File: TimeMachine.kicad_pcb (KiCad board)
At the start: 4 copper layers, 107.6 x 59.8 mm, 52 parts, among them J1 AppleIIBus, J2 JTAG, U1 EPM7128SL84, U2 DS1215, U3 74AHCT04, U4 AS6C8008, U5 39F040, Y1 32k768

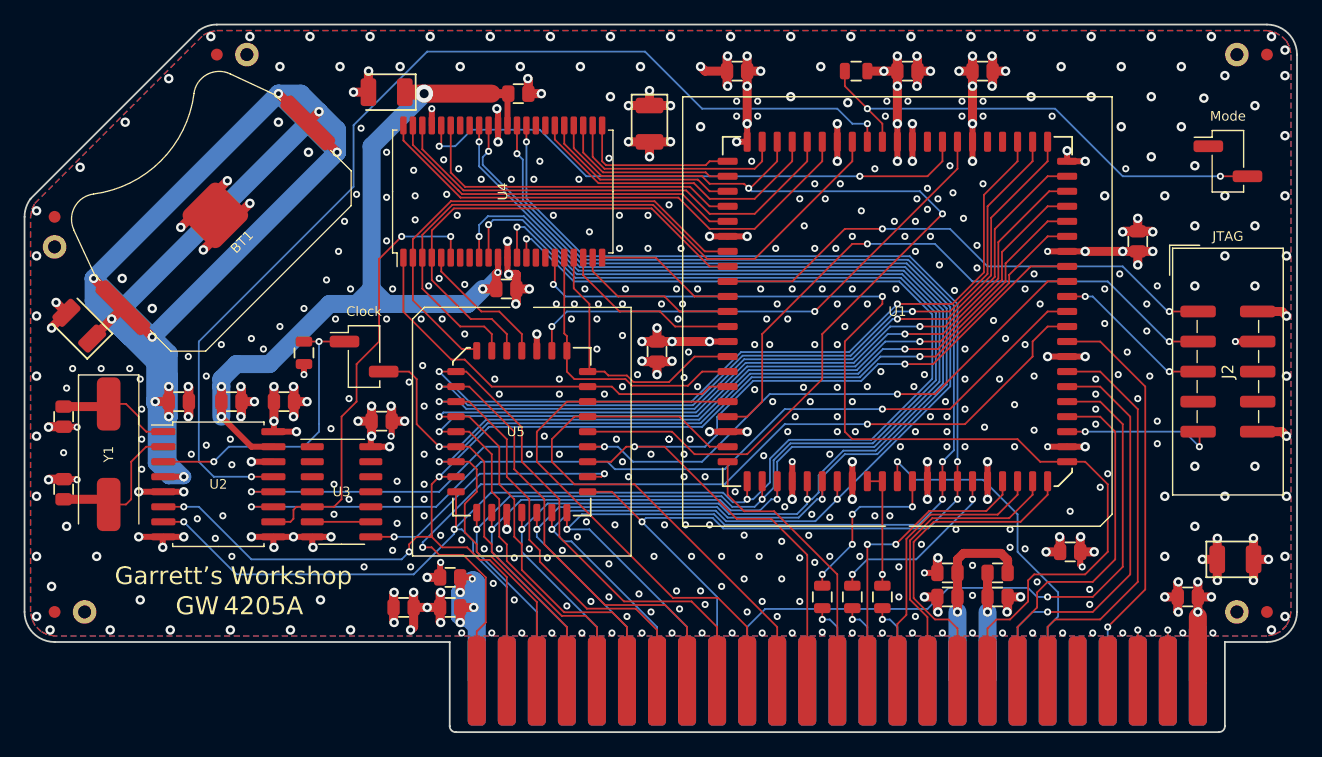
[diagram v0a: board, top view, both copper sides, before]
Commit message: Buffered data bus with CPLD
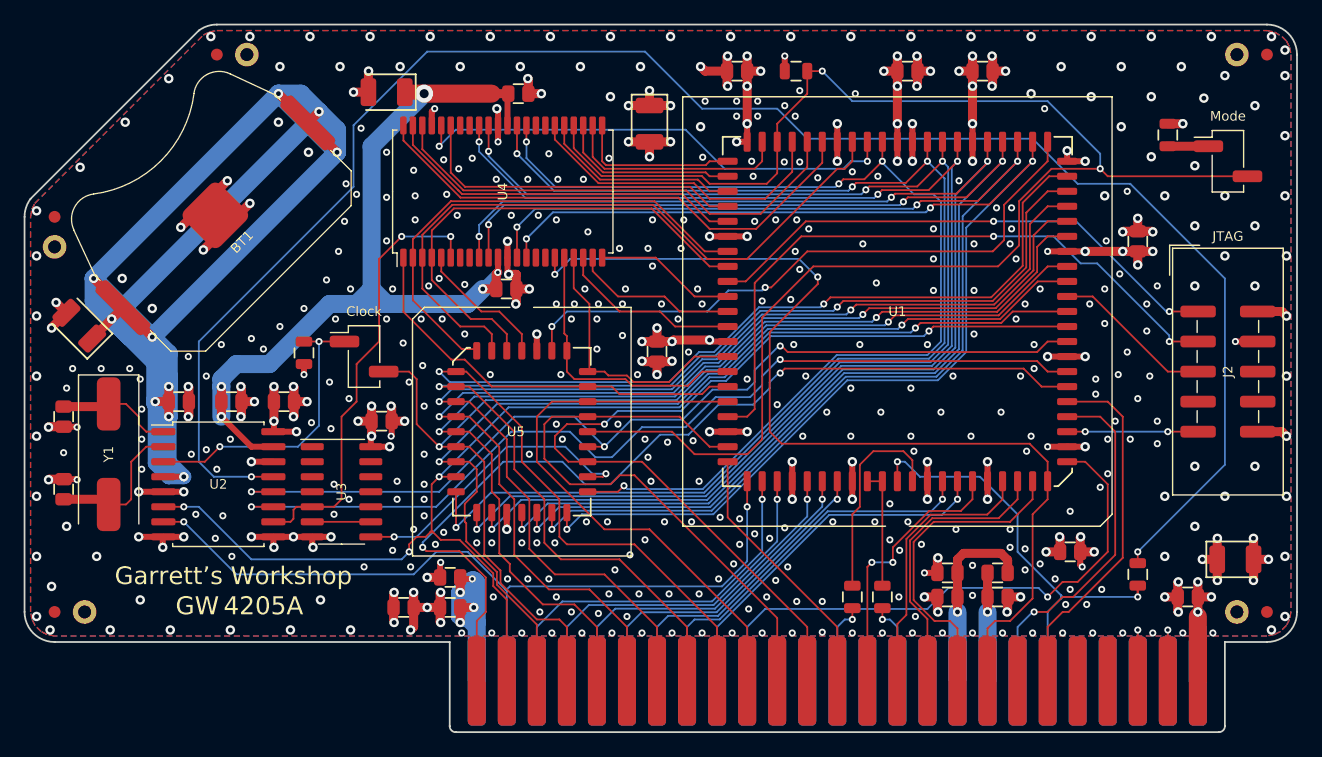
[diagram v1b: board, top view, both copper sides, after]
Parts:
- added R6: 4k7, stdpads:R_0805, F.Cu at (233.7, 126.4)
- R2: value 100 -> 22k
- U3: footprint Package_SO:SOIC-14_3.9x8.7mm_P1.27mm -> stdpads:SOIC-14_3.9mm
- moved R2 44.7 mm to (204.8, 83.8), turned to 0 degrees
- moved R5 26.9 mm to (236.2, 89.2), turned to 90 degrees
- moved R1 2.54 mm to (209.6, 128.3)
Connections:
- net /RAMROMCSgb renamed Net-(U3-Pad6)
- J1 pad 19: /SYNC -> /VIDSYNC
- JP1 pad 1: GND -> Net-(JP1-Pad1)
- JP1 pad 2: /~SMode~ -> /RA11
- R2 pad 1: /Q3r -> GND
- R2 pad 2: /Q3 -> /RA11
- R5 pad 1: /~SMode~ -> Net-(JP1-Pad1)
- U1 pad 10: /A14 -> /A15
- U1 pad 11: /A15 -> /R~W~
- U1 pad 12: /R~W~ -> /~DEVSEL~
- U1 pad 15: /SYNC -> /~INH~
- U1 pad 16: /~DEVSEL~ -> /~IOSTRB~
- U1 pad 17: /~INH~ -> /~IOSEL~
- U1 pad 18: /~IOSTRB~ -> /RAMROM~CS~
- U1 pad 20: /~NMI~ -> /ROM~OE~
- U1 pad 21: /~IOSEL~ -> /A10
- U1 pad 22: /RAMROM~CS~ -> /A0
- U1 pad 24: /ROM~OE~ -> /A1
- U1 pad 25: /A10 -> /A2
- U1 pad 27: /A0 -> /A3
- U1 pad 28: /A1 -> /A4
- U1 pad 29: /A2 -> /A5
- U1 pad 30: /A3 -> /A6
- U1 pad 31: /A4 -> /A7
- U1 pad 33: /A5 -> /ROM~WE~
- U1 pad 34: /A6 -> /RD6
- U1 pad 35: /A7 -> /RD5
- U1 pad 36: Net-(U1-Pad36) -> /RD4
- U1 pad 37: Net-(U1-Pad37) -> /RD3
- U1 pad 39: /ROM~WE~ -> /RD2
- U1 pad 40: /RAMCS -> /RD1
- U1 pad 41: Net-(U1-Pad41) -> /RD0
- U1 pad 44: /~SMode~ -> /RD7
- U1 pad 45: /C~RES~ -> /RAMCS
- U1 pad 6: /Q3r -> /A12
- U1 pad 8: /A12 -> /A13
- U1 pad 9: /A13 -> /A14
- U4 pad 10: /D2 -> /RD4
- U4 pad 13: /D1 -> /RD5
- U4 pad 14: /D0 -> /RD6
- U4 pad 31: /D7 -> /RD7
- U4 pad 32: /D6 -> /RD0
- U4 pad 35: /D5 -> /RD1
- U4 pad 36: /D4 -> /RD2
- U4 pad 9: /D3 -> /RD3
- U5 pad 13: /D0 -> /RD0
- U5 pad 14: /D1 -> /RD1
- U5 pad 15: /D2 -> /RD2
- U5 pad 17: /D3 -> /RD3
- U5 pad 18: /D4 -> /RD4
- U5 pad 19: /D5 -> /RD5
- U5 pad 20: /D6 -> /RD6
- U5 pad 21: /D7 -> /RD7
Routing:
- net /RD4: track 0.00 -> 111.1 mm, vias 0 -> 4
- net /RD3: track 0.00 -> 111.0 mm, vias 0 -> 4
- net /RD2: track 0.00 -> 109.7 mm, vias 0 -> 4
- net /RD5: track 0.00 -> 109.2 mm, vias 0 -> 4
- net /RD6: track 0.00 -> 108.6 mm, vias 0 -> 4
- net /RD1: track 0.00 -> 108.5 mm, vias 0 -> 4
- net /RD0: track 0.00 -> 107.9 mm, vias 0 -> 4
- net /RD7: track 0.00 -> 90.0 mm, vias 0 -> 4
- net /D5: track 114.0 -> 25.8 mm, vias 3 -> 1
- net /D4: track 114.9 -> 27.4 mm, vias 3 -> 1
- net /D6: track 116.6 -> 32.2 mm, vias 4 -> 1
- net /D2: track 114.2 -> 30.4 mm, vias 3 -> 1
- net /D3: track 112.7 -> 29.2 mm, vias 3 -> 1
- net /D7: track 112.8 -> 30.9 mm, vias 4 -> 1
- net /D1: track 110.7 -> 32.2 mm, vias 3 -> 1
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
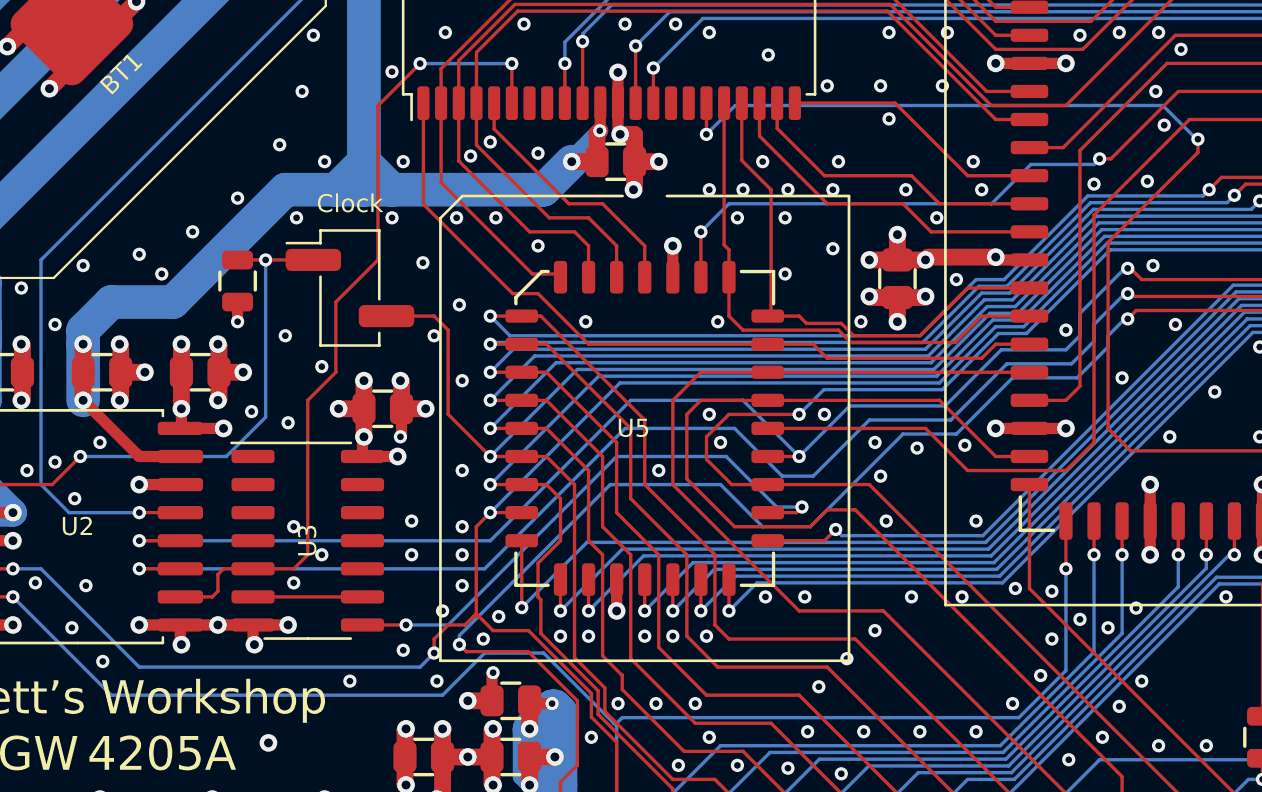
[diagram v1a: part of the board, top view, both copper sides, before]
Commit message: Changed ROM OE strategy
Has gerbers submitted to JLCPCB though
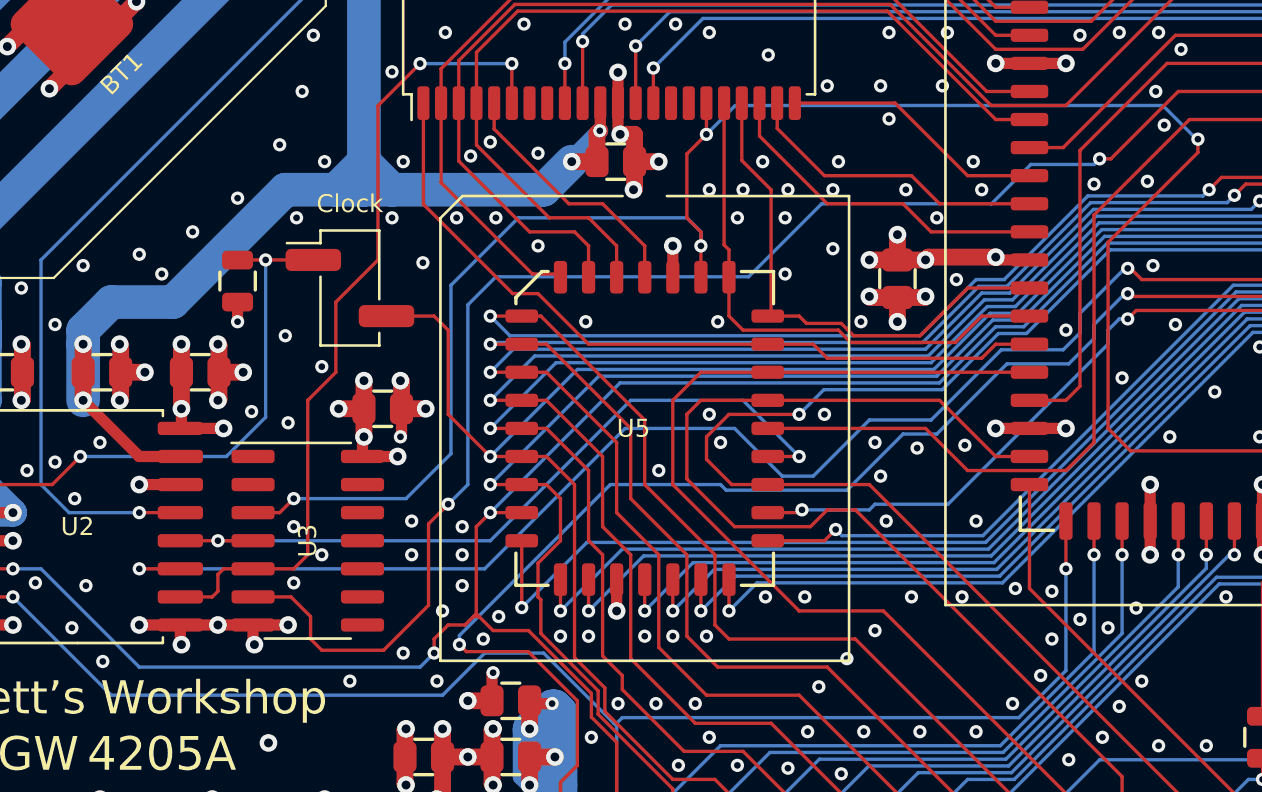
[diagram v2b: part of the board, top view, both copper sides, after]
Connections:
- U1 pad 17: /~IOSEL~ -> /ROM~CS~
- U1 pad 18: /RAMROM~CS~ -> /~IOSEL~
- U1 pad 20: /ROM~OE~ -> /RAMROM~CS~
- U1 pad 33: /ROM~WE~ -> /RAMROMCSgb
- U2 pad 12: /ROM~OE~ -> /~OE~
- U3 pad 3: GND -> /R~W~
- U3 pad 4: Net-(U3-Pad4) -> /~OE~
- U3 pad 6: Net-(U3-Pad6) -> /RAMROMCSgb
- U3 pad 8: /RAMROM~CS~gb -> Net-(U3-Pad8)
- U3 pad 9: Net-(U3-Pad6) -> GND
- U5 pad 22: /RAMROM~CS~gb -> /ROM~CS~
- U5 pad 24: /ROM~OE~ -> /~OE~
- U5 pad 31: /ROM~WE~ -> /R~W~
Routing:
- net /RAMROMCSgb: track 0.00 -> 87.7 mm, vias 0 -> 2
- net /ROM~OE~: track 80.6 -> 0.00 mm, vias 3 -> 0
- net /ROM~WE~: track 53.1 -> 0.00 mm, vias 2 -> 0
- net /ROM~CS~: track 0.00 -> 45.3 mm, vias 0 -> 2
- net /R~W~: track 85.7 -> 123.9 mm, vias 2 -> 4
- net /~OE~: track 0.00 -> 34.7 mm, vias 0 -> 2
- net /RAMROM~CS~gb: track 25.6 -> 0.00 mm, vias 2 -> 0
- net Net-(U3-Pad6): track 4.95 -> 0.00 mm
- net /~IOSEL~: track 79.0 -> 77.8 mm
- net /RAMROM~CS~: track 78.6 -> 79.5 mm
- net GND: vias 483 -> 479

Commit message: Finished layout with new OE stuff.
Updated gerbers and zip
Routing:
- net GND: vias 479 -> 486
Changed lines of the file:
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@@
     (thickness 1.6)
     (drawings 30)
-    (tracks 1921)
+    (tracks 1928)
     (zones 0)
     (modules 53)
@@
   (via (at 233.045 114.935) (size 0.6) (drill 0.3) (layers F.Cu B.Cu) (net 2))
   (via (at 229.616 103.505) (size 0.6) (drill 0.3) (layers F.Cu B.Cu) (net 2))
+  (via (at 172.085 110.109) (size 0.6) (drill 0.3) (layers F.Cu B.Cu) (net 2))
+  (via (at 172.212 108.585) (size 0.6) (drill 0.3) (layers F.Cu B.Cu) (net 2))
+  (via (at 173.482 108.0135) (size 0.6) (drill 0.3) (layers F.Cu B.Cu) (net 2))
+  (via (at 173.101 106.68) (size 0.6) (drill 0.3) (layers F.Cu B.Cu) (net 2))
+  (via (at 175.006 106.68) (size 0.6) (drill 0.3) (layers F.Cu B.Cu) (net 2))
+  (via (at 172.974 116.205) (size 0.6) (drill 0.3) (layers F.Cu B.Cu) (net 2))
+  (via (at 171.196 122.047) (size 0.6) (drill 0.3) (layers F.Cu B.Cu) (net 2))
   (via (at 174.625 113.03) (size 0.6) (drill 0.3) (layers F.Cu B.Cu) (net 3))
   (segment (start 174.625 113.03) (end 176.0475 113.03) (width 0.1524) (layer F.Cu) (net 3))

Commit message: Submitted to JLCPCB
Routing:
- net GND: vias 486 -> 487
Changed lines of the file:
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@@
     (thickness 1.6)
     (drawings 30)
-    (tracks 1928)
+    (tracks 1929)
     (zones 0)
     (modules 53)
@@
   (via (at 172.974 116.205) (size 0.6) (drill 0.3) (layers F.Cu B.Cu) (net 2))
   (via (at 171.196 122.047) (size 0.6) (drill 0.3) (layers F.Cu B.Cu) (net 2))
+  (via (at 168.91 104.775) (size 0.6) (drill 0.3) (layers F.Cu B.Cu) (net 2))
   (via (at 174.625 113.03) (size 0.6) (drill 0.3) (layers F.Cu B.Cu) (net 3))
   (segment (start 174.625 113.03) (end 176.0475 113.03) (width 0.1524) (layer F.Cu) (net 3))
